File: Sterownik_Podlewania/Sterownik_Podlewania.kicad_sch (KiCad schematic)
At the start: 26 parts, among them J10 Conn_01x06_Socket, J11 Conn_01x06_Socket, J3 Conn_01x05_Pin, J4 Conn_01x05_Pin, J5 Conn_01x03_Pin, J7 Conn_01x05_Socket, J8 Conn_01x04_Socket, J9 Conn_01x06_Socket, U1 ESP32-DEVKITC

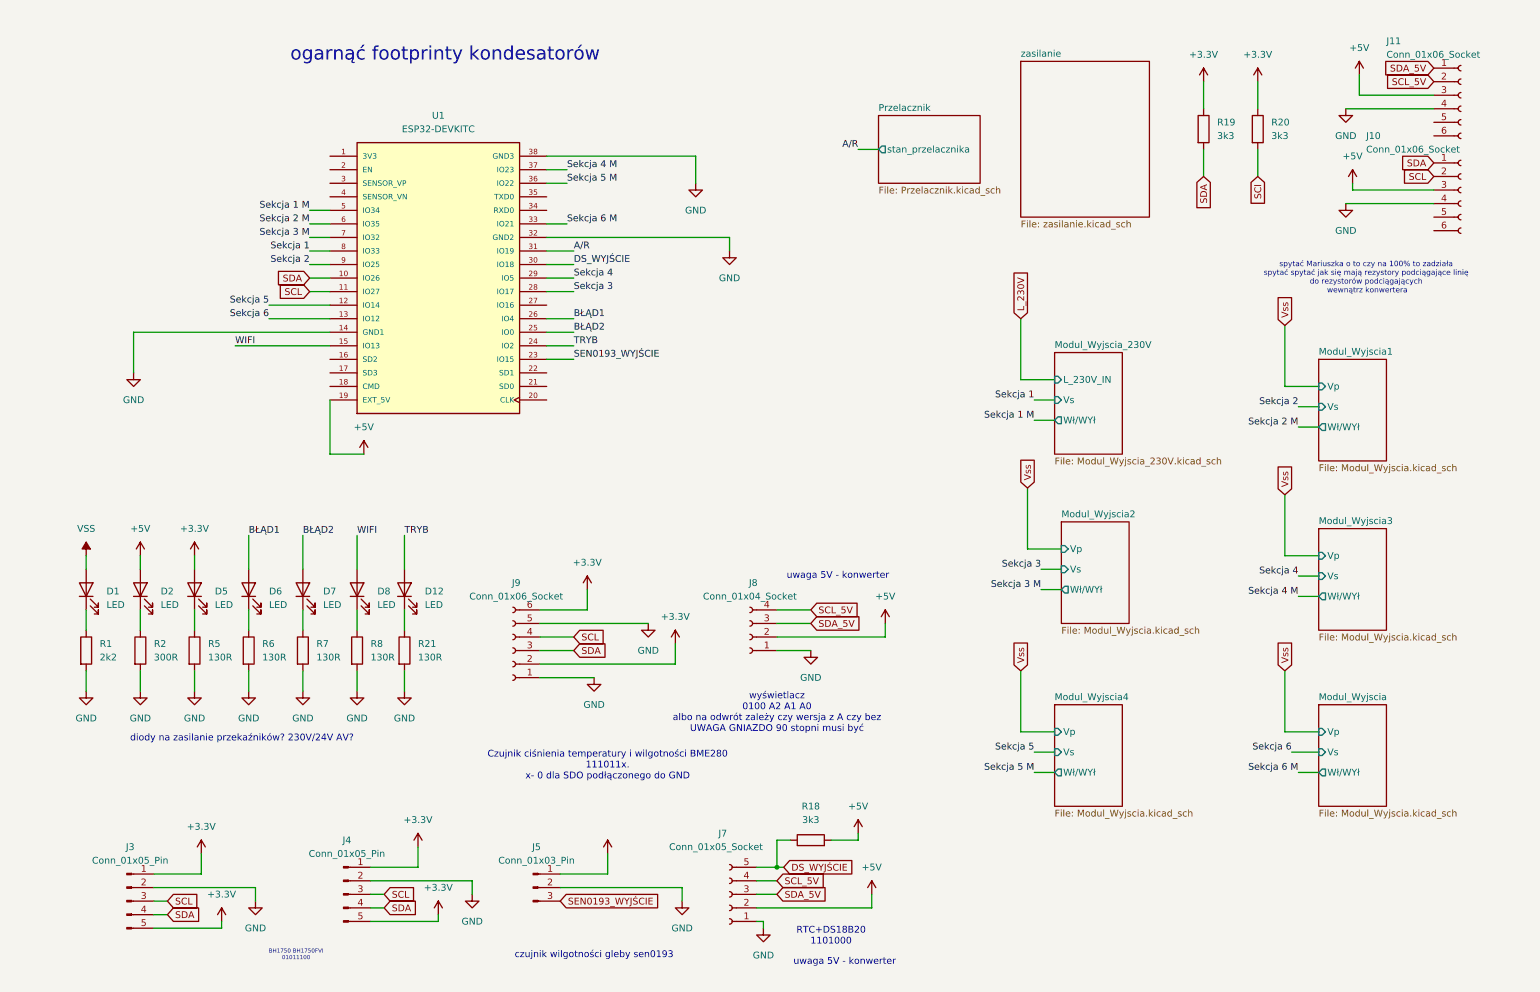
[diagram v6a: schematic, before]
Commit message: Dodanie gniazd ethernet, poprawienie większośc ERC
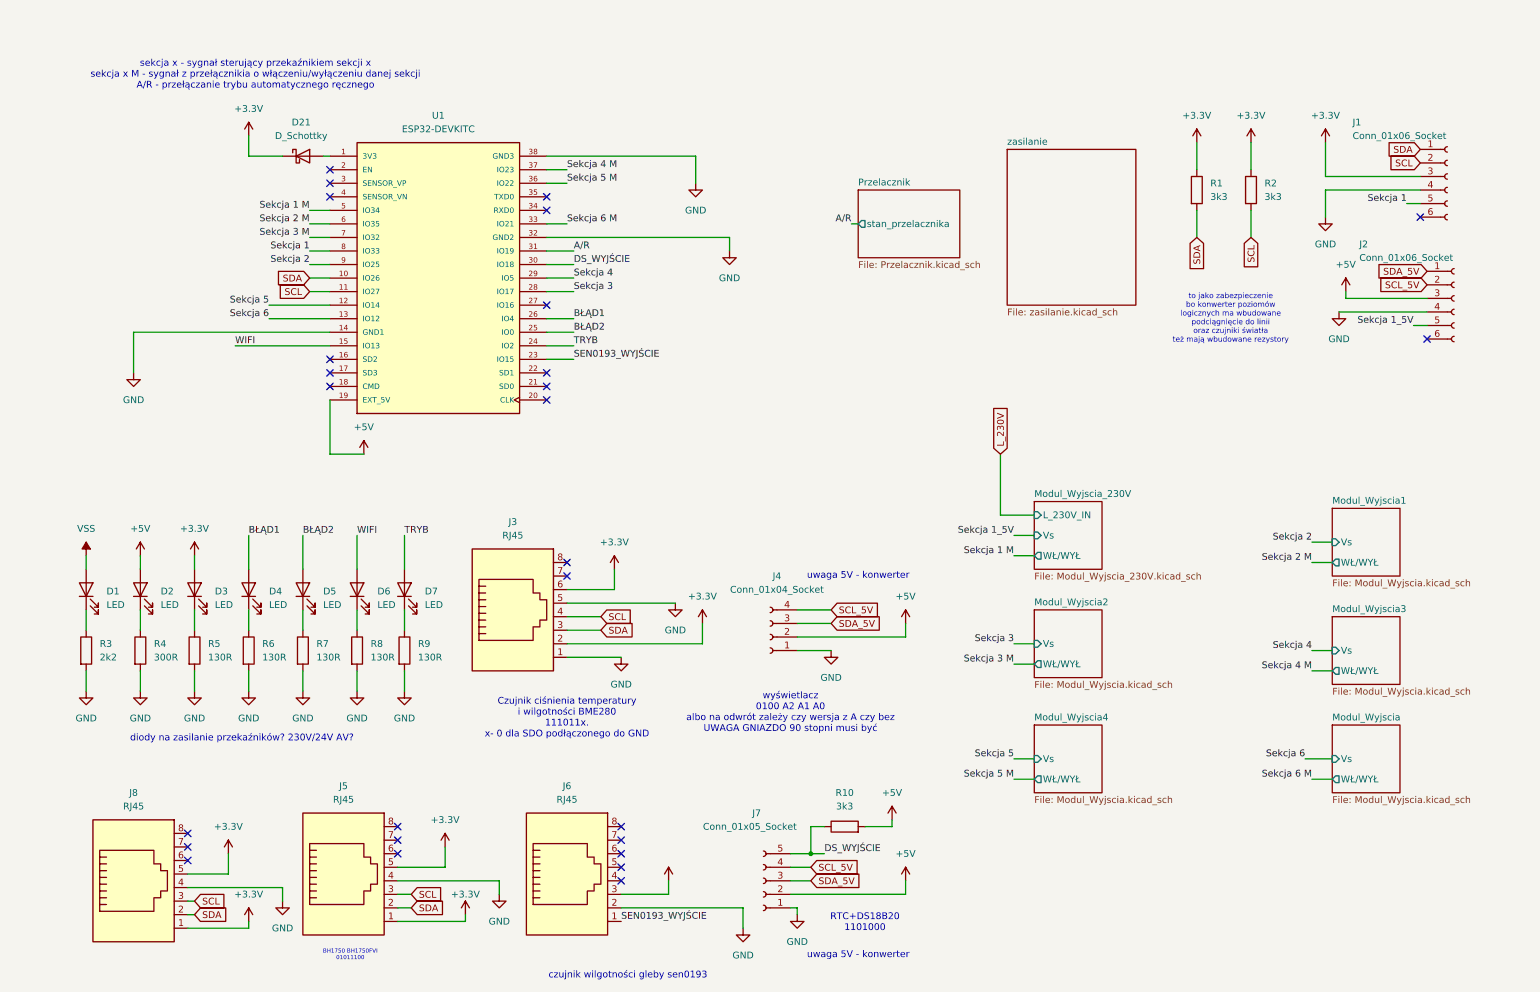
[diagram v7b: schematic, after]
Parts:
- removed J11, J9: Conn_01x06_Socket, Connector_Harwin:Harwin_M20-89006xx_1x06_P2.54mm_Horizontal, symbol Connector:Conn_01x06_Socket
- removed J3, J4: Conn_01x05_Pin, Connector_Harwin:Harwin_M20-89005xx_1x05_P2.54mm_Horizontal, symbol Connector:Conn_01x05_Pin
- removed J5: Conn_01x03_Pin, Connector_Harwin:Harwin_M20-89004xx_1x04_P2.54mm_Horizontal, symbol Connector:Conn_01x03_Pin
- added D21: D_Schottky, symbol Device:D_Schottky
- added J1: Conn_01x06_Socket, Connector_Harwin:Harwin_M20-89006xx_1x06_P2.54mm_Horizontal, symbol Connector:Conn_01x06_Socket
- added J3, J5, J6, J8: RJ45, Connector_RJ:RJ45_Amphenol_54602-x08_Horizontal, symbol Connector:RJ45
- J7: footprint (none) -> Connector_Harwin:Harwin_M20-89005xx_1x05_P2.54mm_Horizontal
- U1: footprint ESP32-DEVKITC:MODULE_ESP32-DEVKITC -> RF_Module:ESP32-C3-DevKitM-1
- renumbered D5 to D3, D6 to D4, D7 to D5, D8 to D6, D12 to D7, J10 to J2, J8 to J4, R19 to R1, R18 to R10, R20 to R2, R1 to R3, R2 to R4, R21 to R9
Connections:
- net SCl is gone; now on net SCL: R2.2
- net +3.3V: now also D21.1 (K), J1.3 (Pin_3), J3.2, J3.6, J5.1, J5.5, J6.3, J8.1, J8.5
- net GND: now also J1.4 (Pin_4), J3.1, J3.5, J5.4, J6.2, J8.4
- net SCL: now also J1.2 (Pin_2), J3.4, J5.3, J8.3; no longer J2.2 (Pin_2)
- net SCL_5V: now also J2.2 (Pin_2)
- net SDA: now also J1.1 (Pin_1), J3.3, J5.2, J8.2; no longer J2.1 (Pin_1)
- net SDA_5V: now also J2.1 (Pin_1)
- net SEN0193_WYJŚCIE: now also J6.1
- net Sekcja 1: now also J1.5 (Pin_5)
- net Sekcja 1_5V: now reaches J2.5 (Pin_5)
- net at U1.1 (3V3): now also D21.2 (A)
- no-connect marks 0 -> 27
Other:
- sheet Modul_Wyjscia ports: added WŁ/WYŁ; removed Vp, Wł/WYł
- sheet Modul_Wyjscia1 ports: added WŁ/WYŁ; removed Vp, Wł/WYł
- sheet Modul_Wyjscia2 ports: added WŁ/WYŁ; removed Vp, Wł/WYł
- sheet Modul_Wyjscia3 ports: added WŁ/WYŁ; removed Vp, Wł/WYł
- sheet Modul_Wyjscia4 ports: added WŁ/WYŁ; removed Vp, Wł/WYł
- sheet Modul_Wyjscia_230V ports: added WŁ/WYŁ; removed Wł/WYł
- note added: "sekcja x - sygnał sterujący przekaźnikiem sekcji x sekcja x M - sygnał z przełącznikia o włączeniu/wyłączeniu danej sekcji A/R - przełączanie trybu automatycznego ręcznego"
- note added: "to jako zabezpieczenie bo konwerter poziomów logicznych ma wbudowane podciągnięcie do linii oraz czujniki światła też mają wbudowane rezystory"
- note removed: "ogarnąć footprinty kondesatorów"
- note removed: "spytać Mariuszka o to czy na 100% to zadziała spytać spytać jak się mają rezystory podciągające linię do rezystorów podciągających wewnątrz konwertera"
- title: Sterownik podlewania -> Sterownik podlewania V1.1
- moved on the sheet: J2, J4, J7, R1, R10, R2

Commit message: Wstępny układ PCB
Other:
- sheet Modul_Wyjscia_230V ports: added none; removed L_230V_IN
- moved on the sheet: J1
